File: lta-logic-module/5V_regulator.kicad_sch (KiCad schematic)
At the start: 8 parts

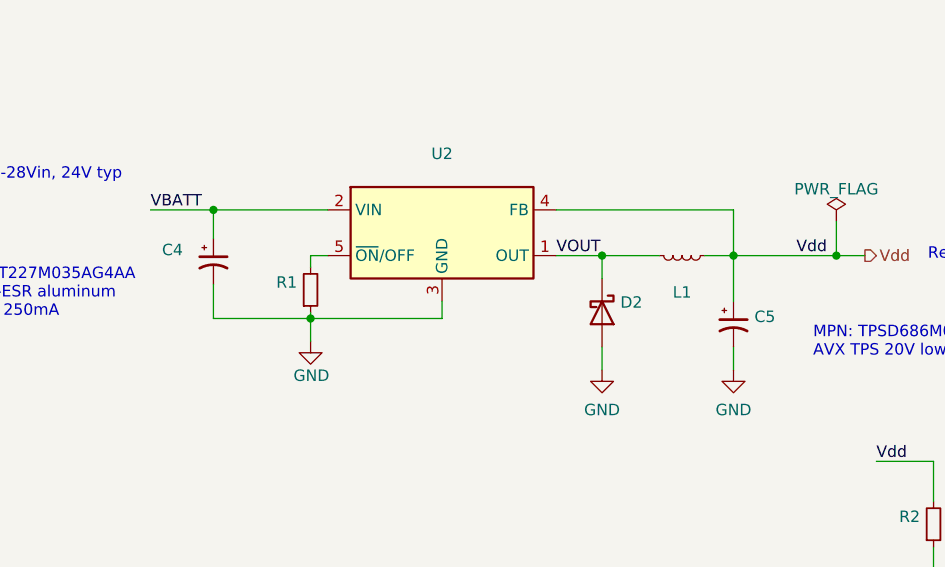
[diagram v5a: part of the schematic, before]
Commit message: Add main draft of PCB layout for logic module.
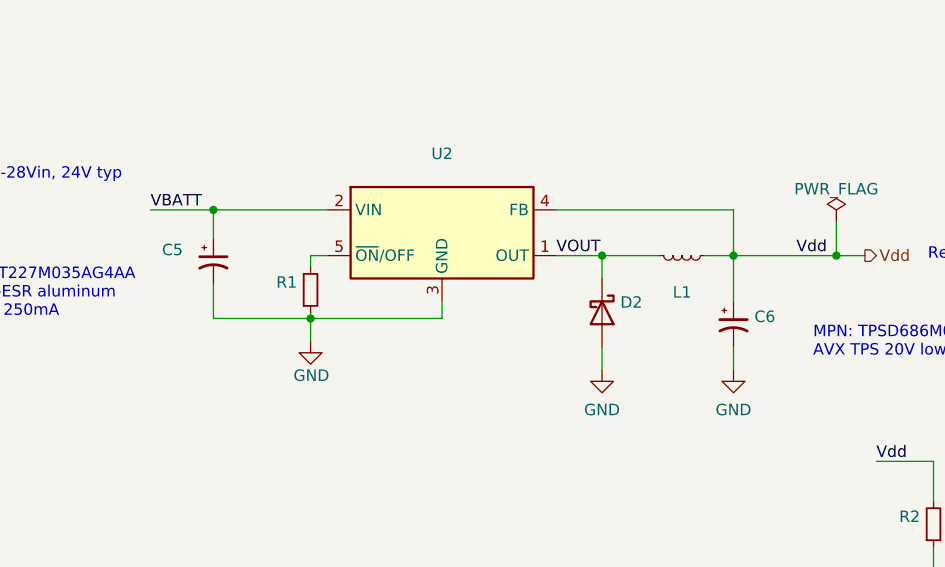
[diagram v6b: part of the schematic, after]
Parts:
- C5: renamed from C4; Comment 35V low-ESR (<=160mOhm), I_RMS>250mA aluminum -> 220u 35V low-ESR (<=160mOhm), I_RMS>250mA aluminum
- C6: renamed from C5; Comment AVX TPS 20V low-ESR (<=150mOhm) solid tantalum -> 68u AVX TPS 20V low-ESR (<=150mOhm) solid tantalum; exact M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; MANUFACTURER Kyocera AVX -> KYOCERA AVX
- D2: Comment (none) -> 30V 5A Schottky diode, Vf <= 480mV. (Any SB530-xxx diode OK)
- L1, U2: Comment (none) -> Exact MFR/MPN required
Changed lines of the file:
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@@
   (symbol (lib_id "Device:C_Polarized_Small_US") (at 96.52 70.485 0) (unit 1)
     (in_bom yes) (on_board yes)
-    (property "Reference" "C4" (id 0) (at 90.805 69.215 0)
+    (property "Reference" "C5" (id 0) (at 90.805 69.215 0)
       (effects (font (size 1.27 1.27)) (justify left))
     )
@@
       (effects (font (size 1.27 1.27)) hide)
     )
-    (property "Comment" "35V low-ESR (<=160mOhm), I_RMS>250mA aluminum" (id 6) (at 96.52 70.485 0)
+    (property "Comment" "220u 35V low-ESR (<=160mOhm), I_RMS>250mA aluminum" (id 6) (at 96.52 70.485 0)
       (effects (font (size 1.27 1.27)) hide)
     )
@@
       (effects (font (size 1.27 1.27)) hide)
     )
+    (property "Comment" "Exact MFR/MPN required" (id 6) (at 148.59 69.85 0)
+      (effects (font (size 1.27 1.27)) hide)
+    )
     (pin "1")
     (pin "2")
@@
     )
     (property "MANUFACTURER" "Vishay" (id 5) (at 139.7 76.2 90)
+      (effects (font (size 1.27 1.27)) hide)
+    )
+    (property "Comment" " 30V 5A Schottky diode, Vf <= 480mV. (Any SB530-xxx diode OK)" (id 6) (at 139.7 76.2 0)
       (effects (font (size 1.27 1.27)) hide)
     )
@@
       (effects (font (size 1.27 1.27)) hide)
     )
+    (property "Comment" "Exact MFR/MPN required" (id 6) (at 121.92 67.31 0)
+      (effects (font (size 1.27 1.27)) hide)
+    )
     (pin "1")
     (pin "2")
@@
   (symbol (lib_id "Device:C_Polarized_Small_US") (at 154.305 77.47 0) (unit 1)
     (in_bom yes) (on_board yes) (fields_autoplaced)
-    (property "Reference" "C5" (id 0) (at 156.6291 76.6416 0)
+    (property "Reference" "C6" (id 0) (at 156.6291 76.6416 0)
       (effects (font (size 1.27 1.27)) (justify left))
     )
@@
       (effects (font (size 1.27 1.27)) hide)
     )
-    (property "MANUFACTURER" "Kyocera AVX" (id 6) (at 154.305 77.47 0)
-      (effects (font (size 1.27 1.27)) hide)
-    )
-    (property "Comment" "AVX TPS 20V low-ESR (<=150mOhm) solid tantalum" (id 4) (at 154.305 77.47 0)
-      (effects (font (size 1.27 1.27)) hide)
-    )
+    (property "MANUFACTURER" "KYOCERA AVX" (id 6) (at 154.305 77.47 0)
+      (effects (font (size 1.27 1.27)) hide)
+    )
+    (property "Comment" "68u AVX TPS 20V low-ESR (<=150mOhm) solid tantalum; exact MPN" (id 4) (at 154.305 77.47 0)
+      (effects (font (size 1.27 1.27)) hide)
+    )

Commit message: Fix all the footprint data.
Somehow my footprint info got clobbered. Reset a bunch of symbol
properties to empty... this info is now all back in place.

* Added 3 fiducial marks
* Added 4 mounting holes
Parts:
- R2: Comment 10K 0603 resistor; +/-1%; 1/10W -> 330R 0603 resistor; +/-1%; 1/10W; MPN RC0603FR-0710KL -> RC0603FR-07330RL
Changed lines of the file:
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@@
       (effects (font (size 1.27 1.27)) hide)
     )
-    (property "Comment" "10K 0603 resistor; +/-1%; 1/10W " (id 4) (at 176.53 99.695 0)
+    (property "Comment" "330R 0603 resistor; +/-1%; 1/10W " (id 4) (at 176.53 99.695 0)
       (effects (font (size 1.27 1.27)) hide)
     )
@@
       (effects (font (size 1.27 1.27)) hide)
     )
-    (property "MPN" "RC0603FR-0710KL" (id 6) (at 176.53 99.695 0)
+    (property "MPN" "RC0603FR-07330RL" (id 6) (at 176.53 99.695 0)
       (effects (font (size 1.27 1.27)) hide)
     )

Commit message: More unfucking.
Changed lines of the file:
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@@
     (pin "1")
-  )
-  (symbol (lib_id "Device:C_Polarized_Small_US") (at 96.52 70.485 0) (unit 1)
-    (in_bom yes) (on_board yes)
-    (property "Reference" "C5" (id 0) (at 90.805 69.215 0)
-      (effects (font (size 1.27 1.27)) (justify left))
-    )
-    (property "Value" "" (id 1) (at 89.535 71.755 0)
-      (effects (font (size 1.27 1.27)) (justify left))
-    )
-    (property "Footprint" "" (id 2) (at 96.52 70.485 0)
-      (effects (font (size 1.27 1.27)) hide)
-    )
-    (property "Datasheet" "https://content.kemet.com/datasheets/KEM_A4010_EST.pdf" (id 3) (at 96.52 70.485 0)
-      (effects (font (size 1.27 1.27)) hide)
-    )
-    (property "MPN" "EST227M035AG4AA" (id 4) (at 96.52 70.485 0)
-      (effects (font (size 1.27 1.27)) hide)
-    )
-    (property "MANUFACTURER" "KEMET" (id 5) (at 96.52 70.485 0)
-      (effects (font (size 1.27 1.27)) hide)
-    )
-    (property "Comment" "220u 35V low-ESR (<=160mOhm), I_RMS>250mA aluminum" (id 6) (at 96.52 70.485 0)
-      (effects (font (size 1.27 1.27)) hide)
-    )
-    (pin "1")
-    (pin "2")
   )
   (symbol (lib_id "Device:R_Small") (at 107.315 73.66 0) (mirror x) (unit 1)
@@
       (effects (font (size 1.27 1.27)) hide)
     )
+    (pin "1")
+    (pin "2")
+  )
+  (symbol (lib_id "Device:C_Polarized_Small_US") (at 96.52 70.485 0) (unit 1)
+    (in_bom yes) (on_board yes) (fields_autoplaced)
+    (property "Reference" "C5" (id 0) (at 98.8314 69.2185 0)
+      (effects (font (size 1.27 1.27)) (justify left))
+    )
+    (property "Value" "" (id 1) (at 98.8314 71.7554 0)
+      (effects (font (size 1.27 1.27)) (justify left))
+    )
+    (property "Footprint" "" (id 2) (at 96.52 70.485 0)
+      (effects (font (size 1.27 1.27)) hide)
+    )
+    (property "Datasheet" "https://content.kemet.com/datasheets/KEM_A4010_EST.pdf" (id 3) (at 96.52 70.485 0)
+      (effects (font (size 1.27 1.27)) hide)
+    )
+    (property "MPN" "EST227M035AG4AA" (id 5) (at 96.52 70.485 0)
+      (effects (font (size 1.27 1.27)) hide)
+    )
+    (property "MANUFACTURER" "KEMET" (id 6) (at 96.52 70.485 0)
+      (effects (font (size 1.27 1.27)) hide)
+    )
+    (property "Comment" "220u 35V low-ESR (<=160mOhm), I_RMS>250mA aluminum" (id 4) (at 96.52 70.485 0)
+      (effects (font (size 1.27 1.27)) hide)
+    )
